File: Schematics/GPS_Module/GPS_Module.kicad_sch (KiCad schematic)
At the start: 72 parts, among them J1 GT8E-6P-2H(55), J2 SWD_01x04_Pin, J4 Stack Male Edge Connector, J4 USB_C_Female_USB2_Small, Q1 AO3400A, SW1 SW_STM_RESET, SW2 SW_STM_BOOT_MODE, U1 CP2102N-Axx-xQFN28, U1 STM32F103CBT6, U12 AMS1117-3.3, U2 W25Q128JVS, U4 LM66100DCKR, U5 LM66100DCKR, U6 LM66100DCKR, U9 ISO1042BQDWVR, Y1 X322516MMB4SI

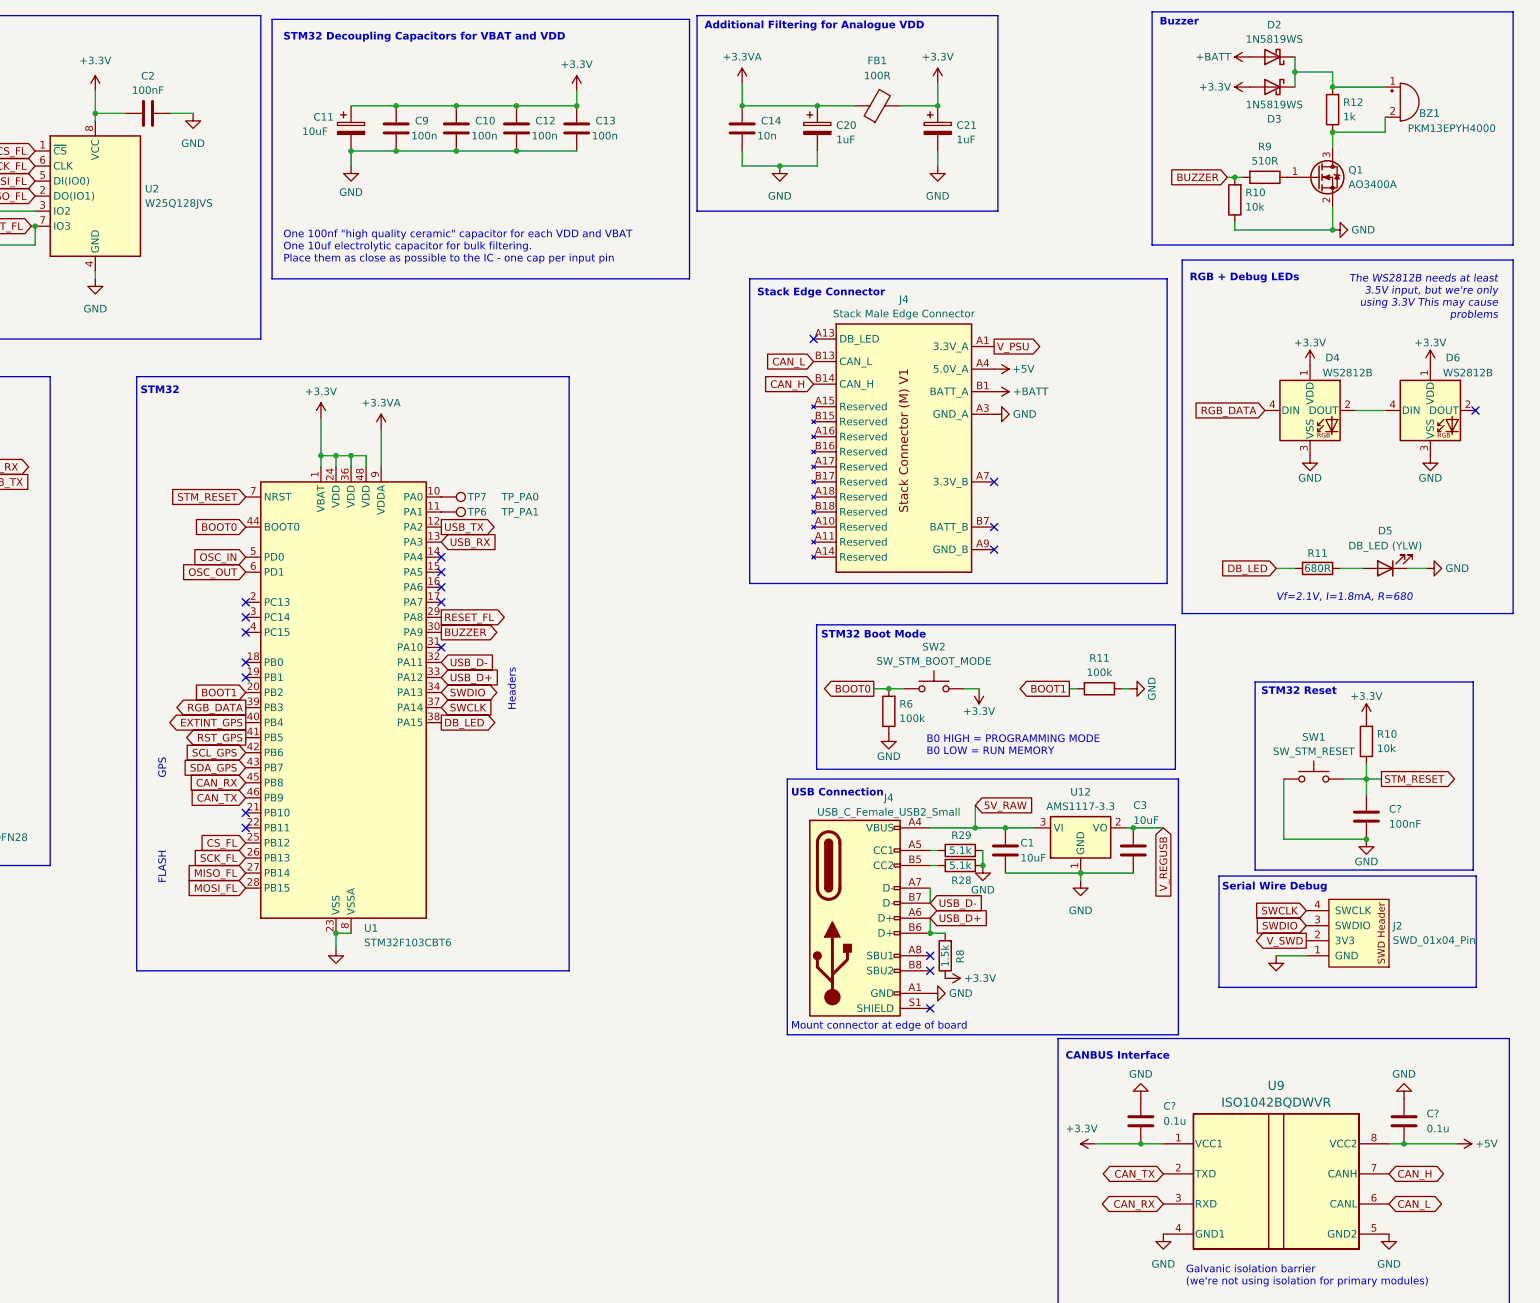
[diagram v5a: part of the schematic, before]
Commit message: Added improved buzzer driver circuit
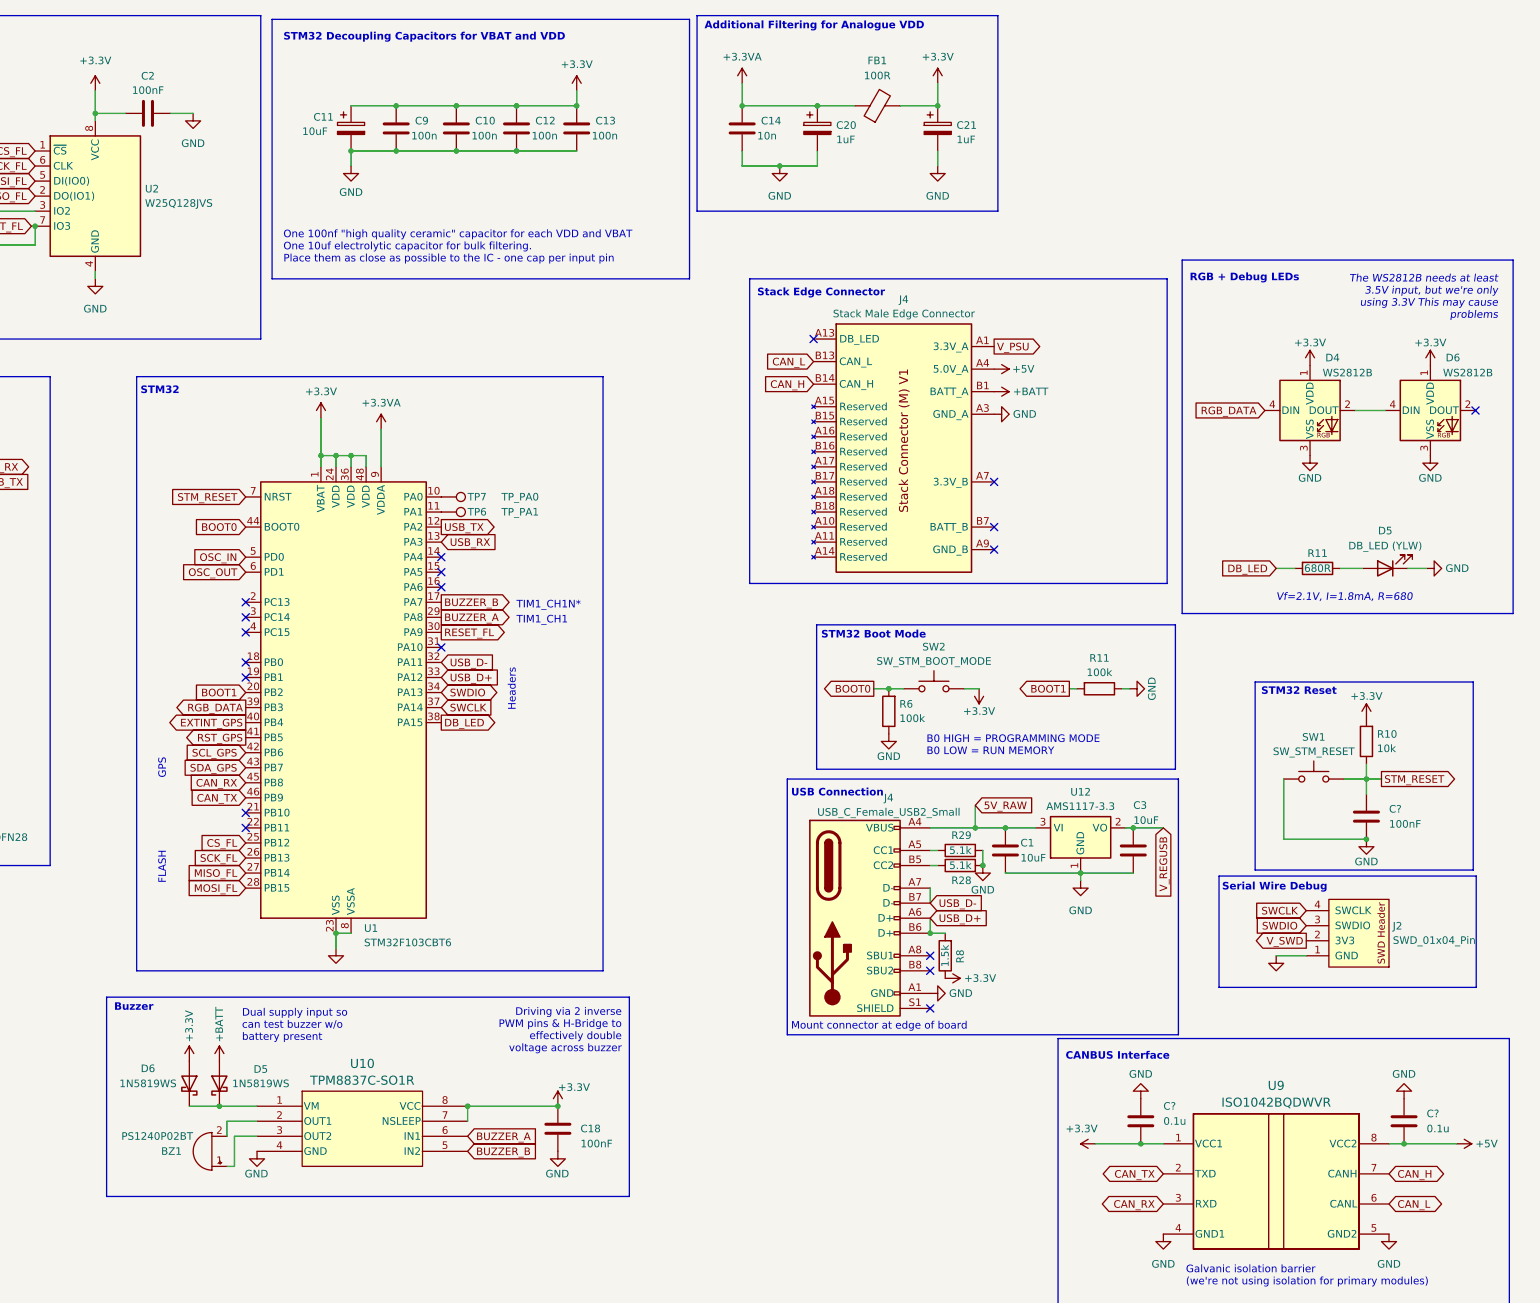
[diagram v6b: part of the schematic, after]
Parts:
- removed D2, D3: 1N5819WS, Diode_SMD:D_SOD-323, symbol Diode:1N5819WS
- removed Q1: AO3400A, Package_TO_SOT_SMD:SOT-23, symbol Transistor_FET:AO3400A
- removed R10: 10k, Resistor_SMD:R_0603_1608Metric, symbol Device:R
- removed R12: 1k, Resistor_SMD:R_0603_1608Metric, symbol Device:R
- removed R9: 510R, Resistor_SMD:R_0603_1608Metric, symbol Device:R
- added C18: 100nF, Capacitor_SMD:C_0603_1608Metric, symbol Device:C
- added D5, D6: 1N5819WS, Diode_SMD:D_SOD-323, symbol Diode:1N5819WS
- added U10: TPM8837C-SO1R, footprints:SOP-8_TPK, symbol TPM8837C-SO1R:TPM8837C-SO1R
- BZ1: value PKM13EPYH4000 -> PS1240P02BT; Digikey 490-4698-1-ND -> 445-2525-1-ND
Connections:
- net BUZZER is gone; now on net RESET_FL: U1.30 (PA9)
- net +3.3V: now also C18.1, D6.2 (A), U10.7 (NSLEEP), U10.8 (VCC)
- net +BATT: now also D5.2 (A)
- net GND: now also C18.2, U10.4 (GND)
- net RESET_FL: no longer U1.29 (PA8)
- net at BZ1.1 (-): now also U10.3 (OUT2)
- net BUZZER_B: now reaches U1.17 (PA7)
- net BUZZER_B: now also U10.5 (IN2)
- net at BZ1.2 (+): now also U10.2 (OUT1)
- new net: D5.1 (K), D6.1 (K), U10.1 (VM)
- new net BUZZER_A: U1.29 (PA8), U10.6 (IN1)
- no-connect marks 38 -> 37
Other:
- note added: "Driving via 2 inverse PWM pins & H-Bridge to effectively double voltage across buzzer"
- note added: "Dual supply input so can test buzzer w/o battery present"
- note added: "TIM1_CH1"
- note added: "TIM1_CH1N*"

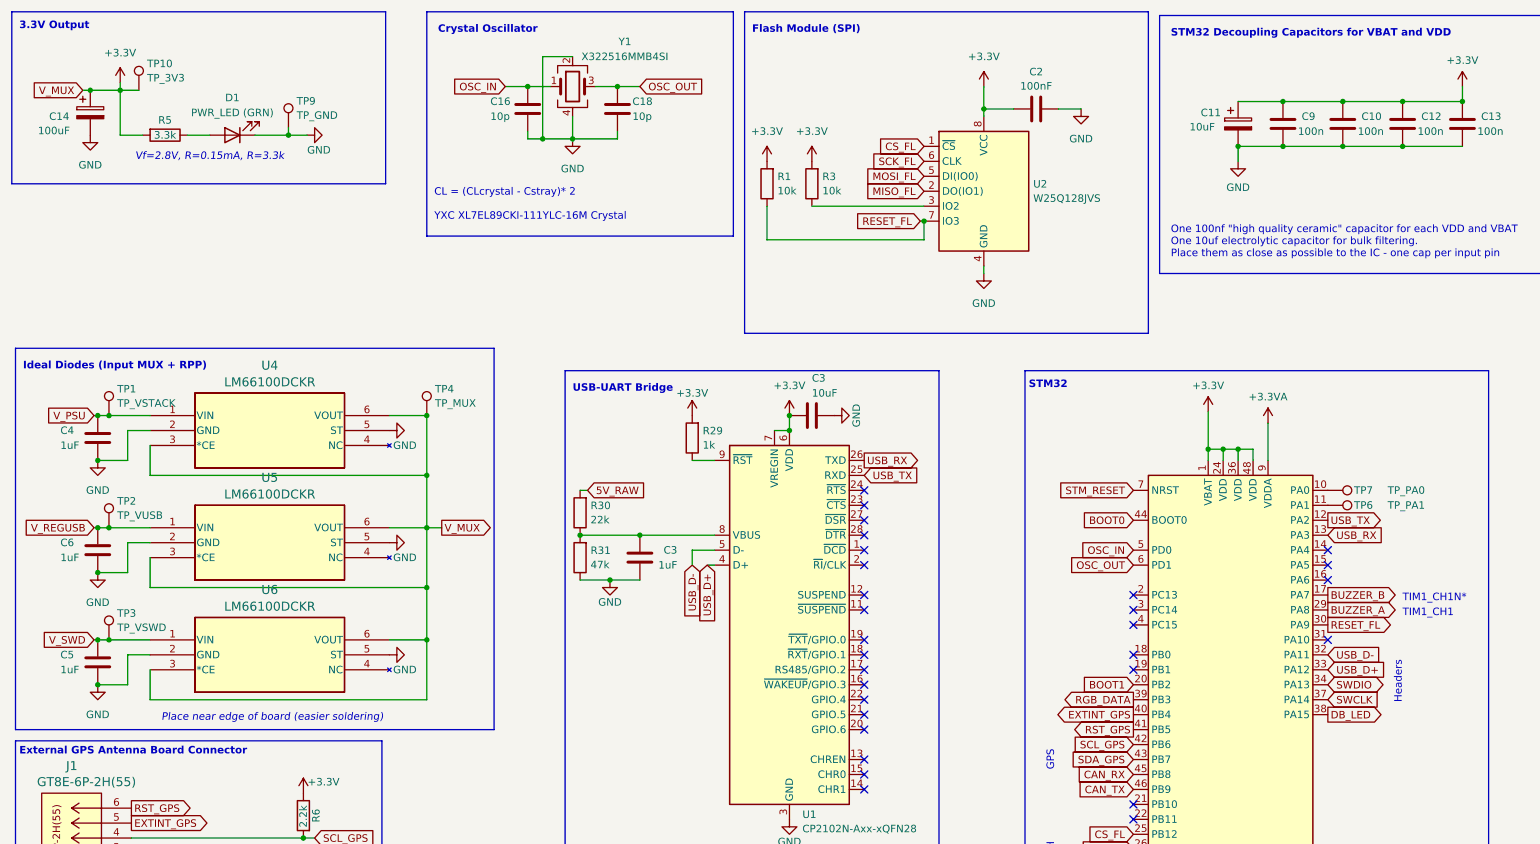
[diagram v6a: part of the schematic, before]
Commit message: Completed GPS module PCB layout
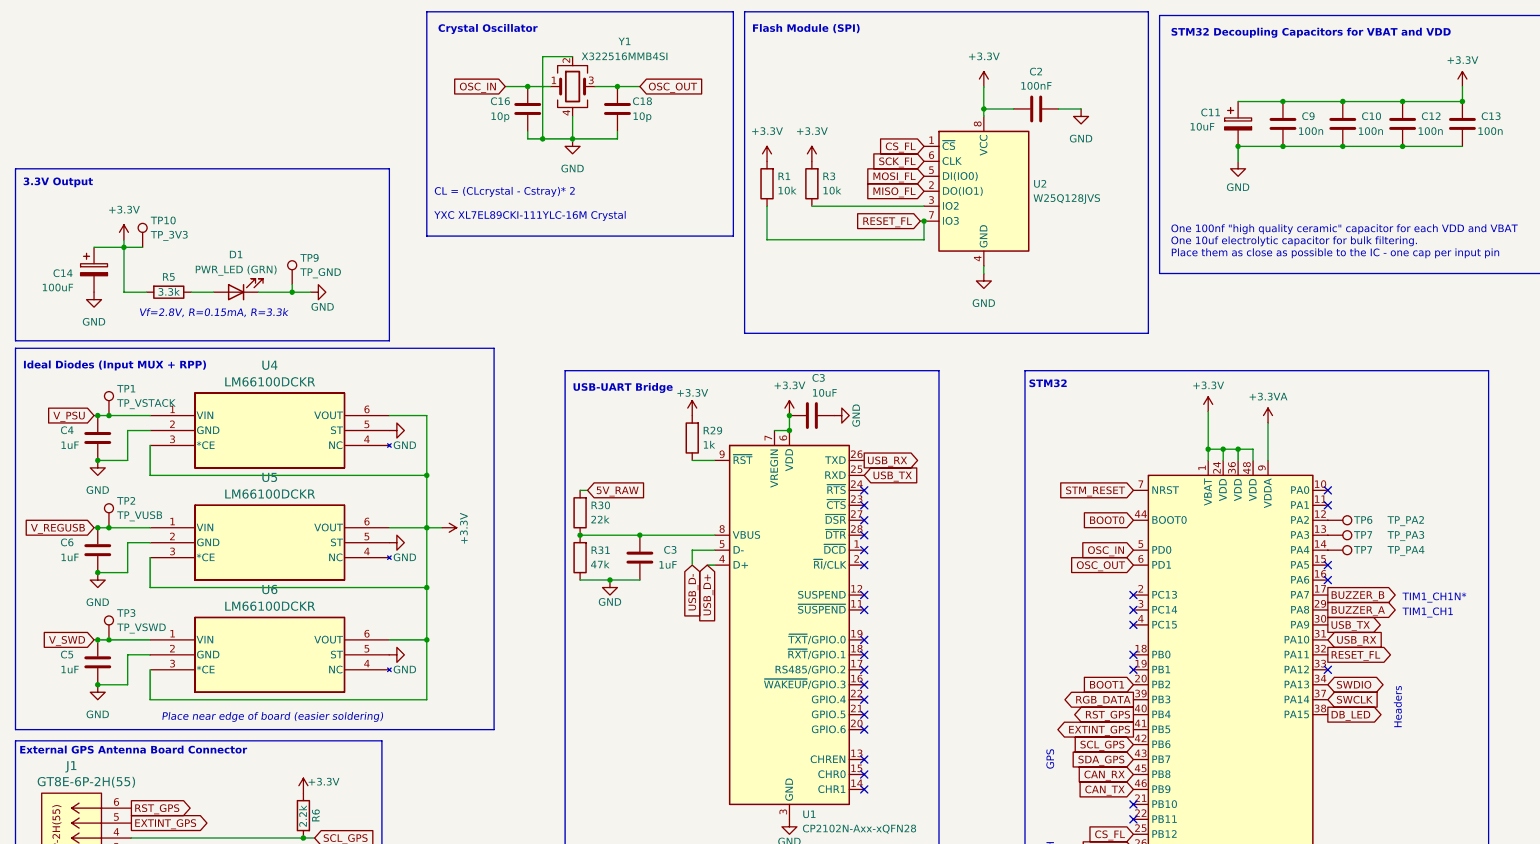
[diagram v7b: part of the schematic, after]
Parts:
- removed TP4: TP_MUX, TestPoint:TestPoint_Pad_1.5x1.5mm, symbol Connector:TestPoint
- added TP7: TP_PA4, TestPoint:TestPoint_Pad_1.5x1.5mm, symbol Connector:TestPoint
- TP6: value TP_PA1 -> TP_PA2
- TP7: value TP_PA0 -> TP_PA3
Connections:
- net EXTINT_GPS: now also U1.41 (PB5); no longer U1.40 (PB4)
- net RESET_FL: now also U1.32 (PA11); no longer U1.30 (PA9)
- net RST_GPS: now also U1.40 (PB4); no longer U1.41 (PB5)
- net USB_D+: no longer U1.33 (PA12)
- net USB_D-: no longer U1.32 (PA11)
- net USB_RX: now also U1.31 (PA10); no longer U1.13 (PA3)
- net USB_TX: now also U1.30 (PA9); no longer U1.12 (PA2)
- net at TP7.1: now also U1.13 (PA3); no longer U1.10 (PA0)
- net at TP6.1: now also U1.12 (PA2); no longer U1.11 (PA1)
- net at U1.14 (PA4): now also TP7.1
- no-connect marks 37 -> 38
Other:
- moved on the sheet: C14, D1, R5, TP10, TP6, TP7, TP9

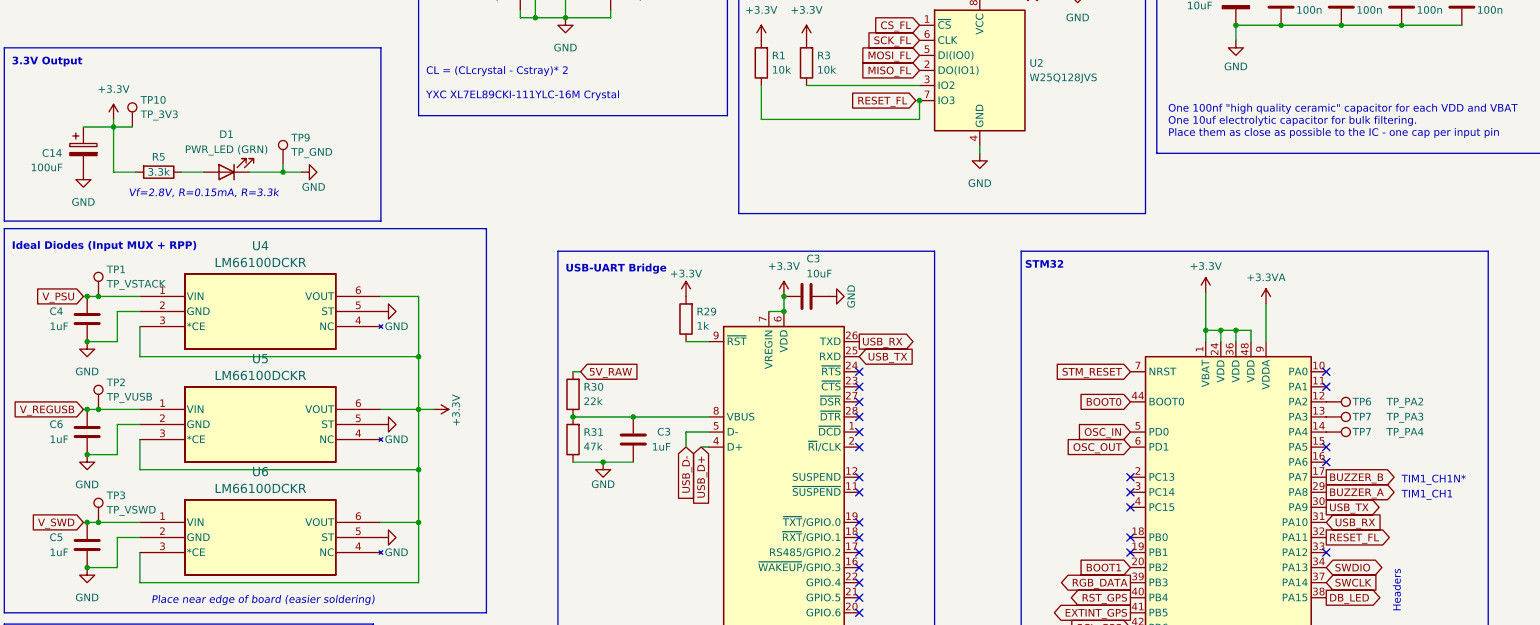
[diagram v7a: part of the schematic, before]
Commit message: Adjustments to GPS Module
- Changed to new USB-C port (C5178541)
- Added version number to front silkscreen
- Adjusted date silkscreen
- Added proper silkscreen labels to test points
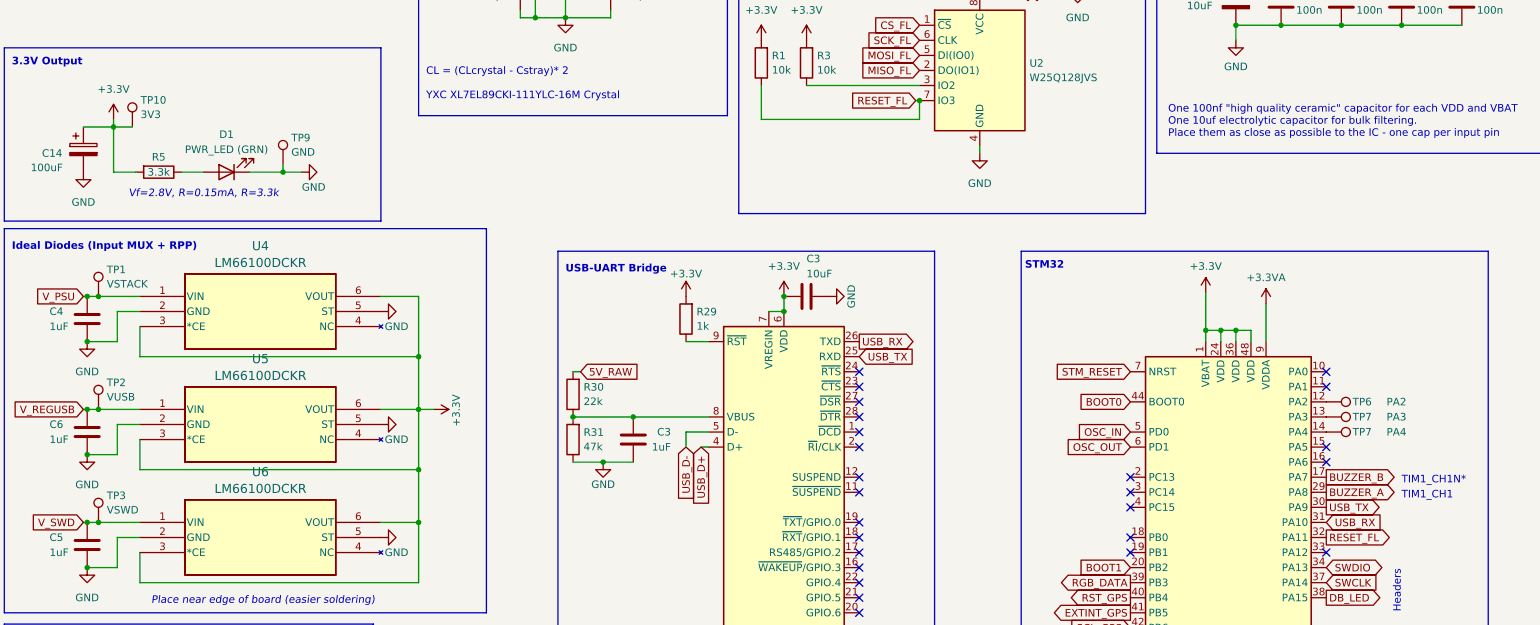
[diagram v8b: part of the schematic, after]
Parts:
- J4: JLCPCB C2936184 -> C5178541
- TP1: value TP_VSTACK -> VSTACK
- TP10: value TP_3V3 -> 3V3
- TP2: value TP_VUSB -> VUSB
- TP3: value TP_VSWD -> VSWD
- TP6: value TP_PA2 -> PA2
- TP7: value TP_PA3 -> PA3
- TP7: value TP_PA4 -> PA4
- TP9: value TP_GND -> GND
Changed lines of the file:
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@@
   (title_block
     (title "QRET 23-25 SRAD GPS Module")
-    (date "2025-02-23")
+    (date "2025-03-06")
     (rev "V2.0")
     (company "Queen's Rocket Engineering Team")
@@
       (effects (font (size 1.27 1.27)) (justify left))
     )
-    (property "Value" "TP_3V3" (at 37.592 51.8851 0)
+    (property "Value" "3V3" (at 37.592 51.8851 0)
       (effects (font (size 1.27 1.27)) (justify left))
     )
@@
       (effects (font (size 1.27 1.27)) (justify left))
     )
-    (property "Value" "TP_PA3" (at 247.65 102.87 90)
+    (property "Value" "PA3" (at 247.65 102.87 90)
       (effects (font (size 1.27 1.27)) (justify left))
     )
@@
       (effects (font (size 1.27 1.27)) (justify left))
     )
-    (property "Value" "TP_PA2" (at 247.65 100.33 90)
+    (property "Value" "PA2" (at 247.65 100.33 90)
       (effects (font (size 1.27 1.27)) (justify left))
     )
@@
       (effects (font (size 1.27 1.27)) (justify left))
     )
-    (property "Value" "TP_VSTACK" (at 31.877 80.4601 0)
+    (property "Value" "VSTACK" (at 31.877 80.4601 0)
       (effects (font (size 1.27 1.27)) (justify left))
     )
@@
       (effects (font (size 1.27 1.27)) (justify left))
     )
-    (property "Value" "TP_PA4" (at 247.65 105.41 90)
+    (property "Value" "PA4" (at 247.65 105.41 90)
       (effects (font (size 1.27 1.27)) (justify left))
     )
@@
       (effects (font (size 1.27 1.27)) (justify left))
     )
-    (property "Value" "TP_GND" (at 62.992 58.2351 0)
+    (property "Value" "GND" (at 62.992 58.2351 0)
       (effects (font (size 1.27 1.27)) (justify left))
     )
@@
       (effects (font (size 1.27 1.27)) hide)
     )
-    (property "JLCPCB" "C2936184" (at 304.8 167.64 0)
+    (property "JLCPCB" "C5178541" (at 304.8 167.64 0)
       (effects (font (size 1.27 1.27)) hide)
     )
@@
       (effects (font (size 1.27 1.27)) (justify left))
     )
-    (property "Value" "TP_VSWD" (at 31.877 118.5601 0)
+    (property "Value" "VSWD" (at 31.877 118.5601 0)
       (effects (font (size 1.27 1.27)) (justify left))
     )
@@
       (effects (font (size 1.27 1.27)) (justify left))
     )
-    (property "Value" "TP_VUSB" (at 31.877 99.5101 0)
+    (property "Value" "VUSB" (at 31.877 99.5101 0)
       (effects (font (size 1.27 1.27)) (justify left))
     )
